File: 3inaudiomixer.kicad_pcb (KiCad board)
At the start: 2 copper layers, 64 x 72 mm, 44 parts, among them J1 AudioJack3, J2 AudioJack3, J3 AudioJack3, J4 AudioJack3, U1 LF353D, U2 LF353D, U3 L78L05_SOT89, U4 L79L05_SOT89

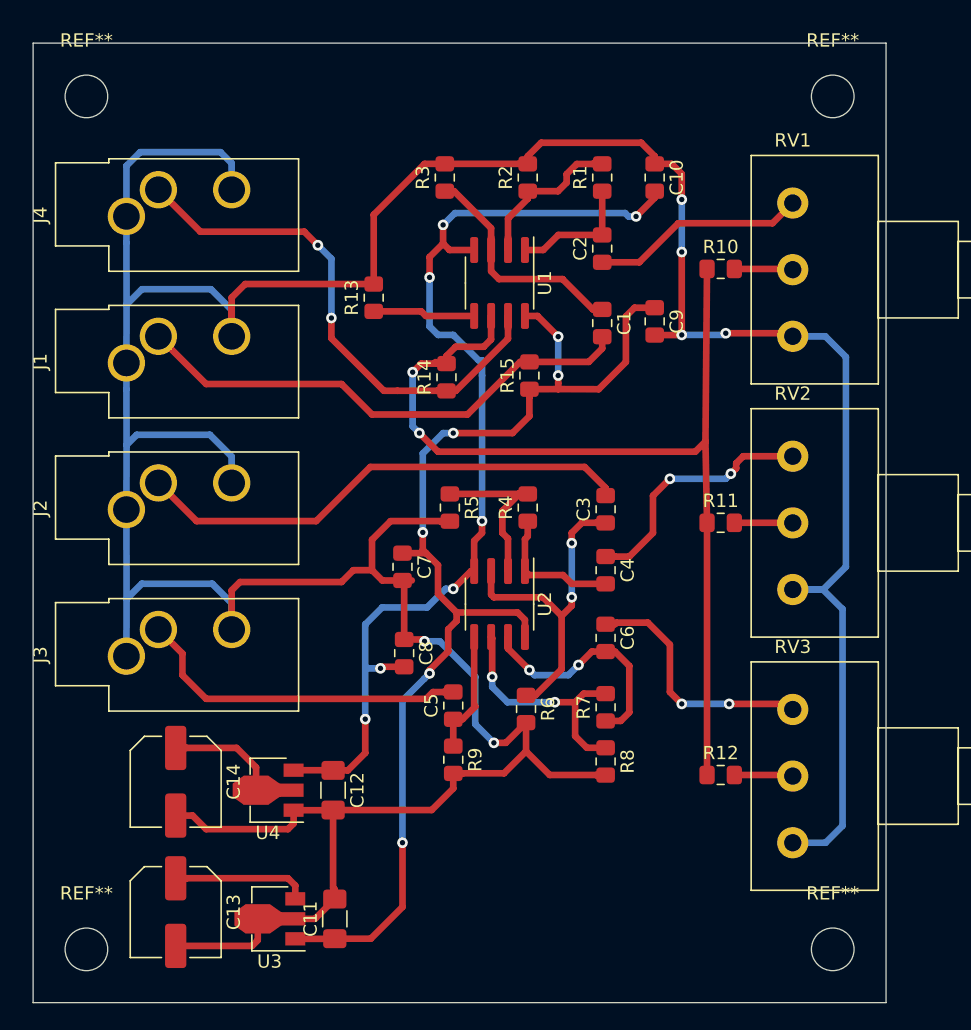
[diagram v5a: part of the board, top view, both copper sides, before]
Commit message: all traces routed & ground planes
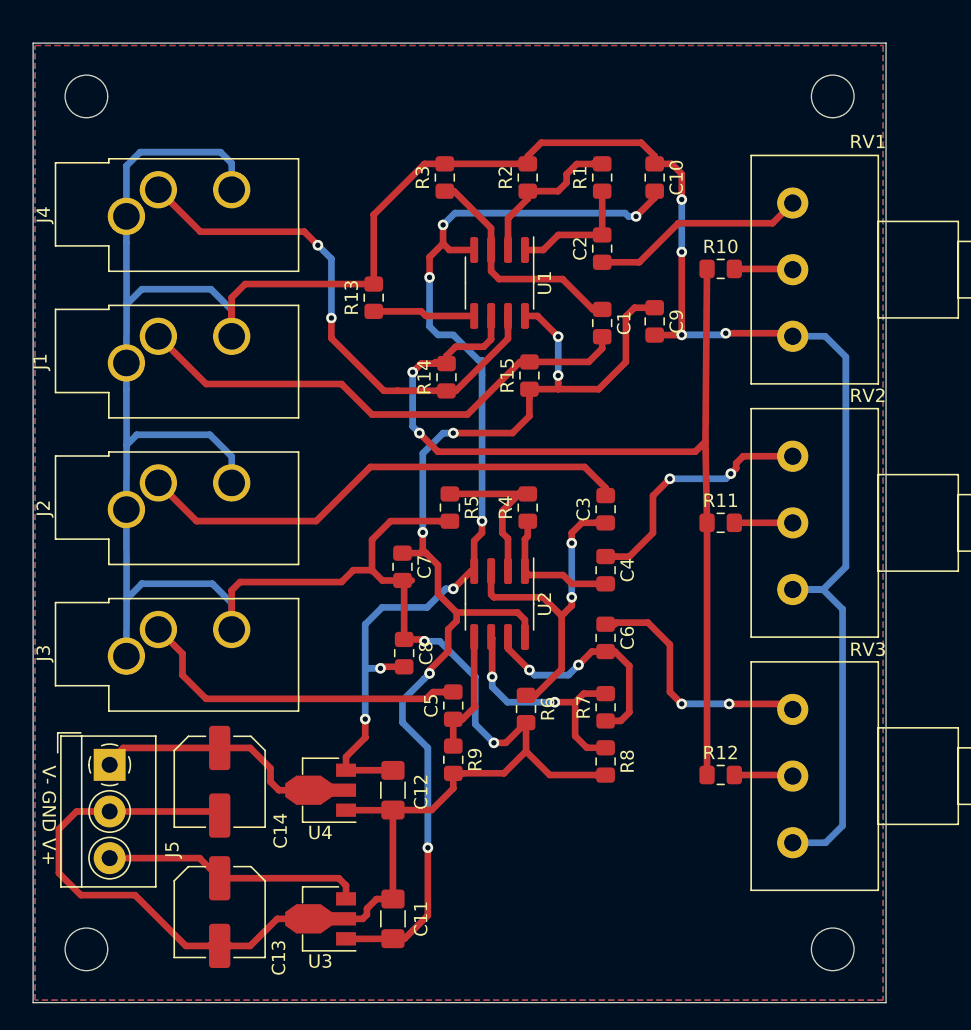
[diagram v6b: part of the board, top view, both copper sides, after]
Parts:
- added J5: Conn_01x03_Female, TerminalBlock_4Ucon:TerminalBlock_4Ucon_1x03_P3.50mm_Horizontal, F.Cu at (118.7, 97.2)
- moved C12 4.49 mm to (140.0, 99.1)
- moved C11 4.36 mm to (140.0, 108.7)
- moved U4 3.94 mm to (135.0, 99.1)
- moved U3 3.81 mm to (135.0, 108.7)
- moved C13 3.30 mm to (127.0, 108.2)
- moved C14 3.30 mm to (127.0, 98.4)
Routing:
- net Net-(C10-Pad1): track 308.7 -> 323.7 mm
- net Net-(C13-Pad1): track 10.2 -> 19.6 mm
- net Net-(C14-Pad1): track 12.4 -> 20.2 mm
- net Net-(C11-Pad1): track 86.4 -> 85.7 mm
- net Net-(C10-Pad2): track 77.5 -> 77.0 mm
- added copper zone on B.Cu, net Net-(C10-Pad1)
- added copper zone on F.Cu, net Net-(C10-Pad1)
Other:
- board text added: "V- GND V+"

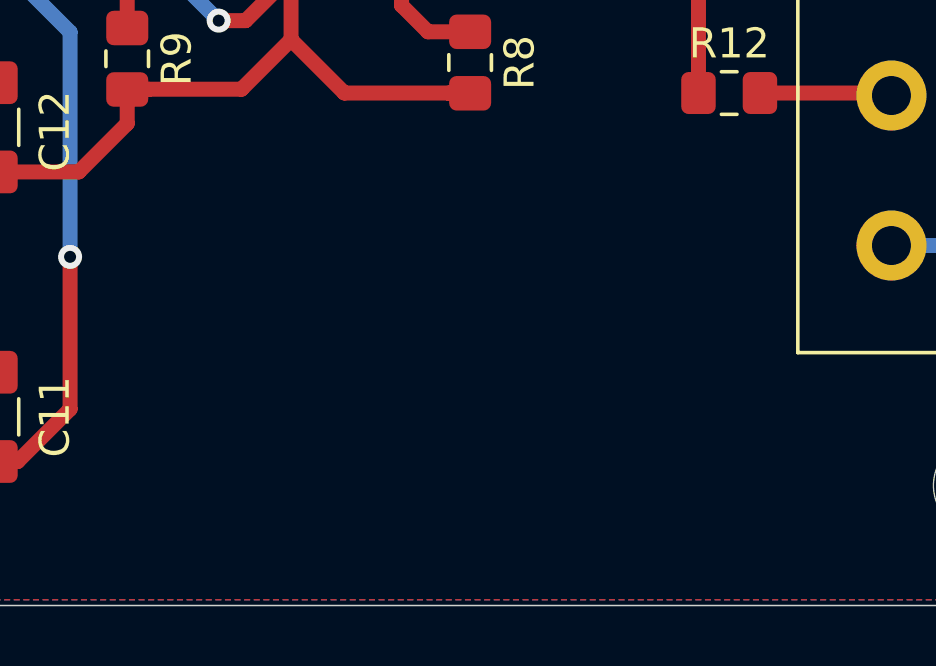
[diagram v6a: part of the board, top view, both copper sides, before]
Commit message: scaled down logo
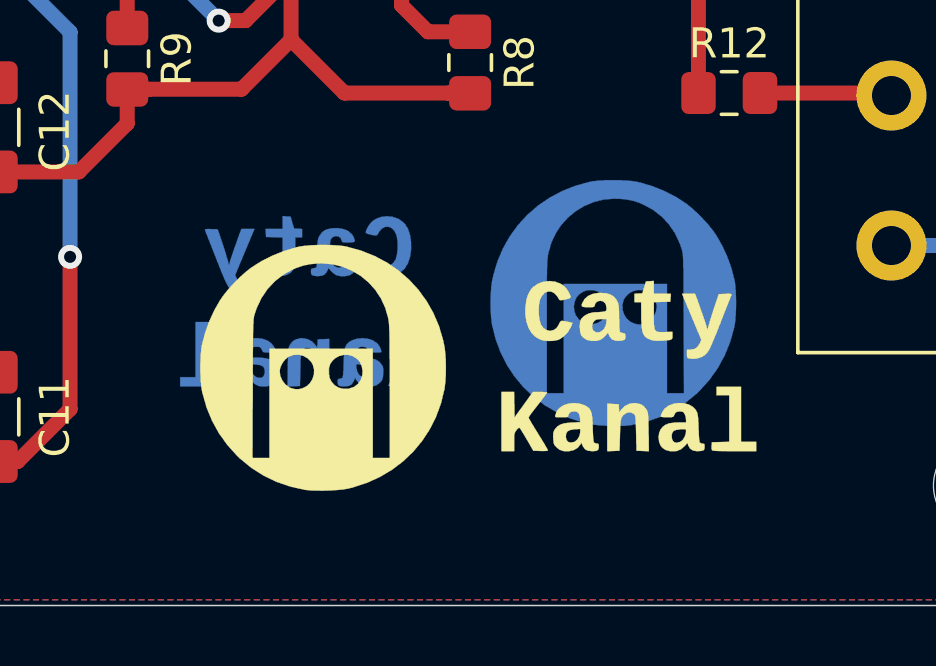
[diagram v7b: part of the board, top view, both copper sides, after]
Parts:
- added G***: LOGO, Logos_Caty_Kanal:CATY-KANAL-Logo_18x8mm_Copper, B.Cu at (155.6, 104.9)
- added G***: LOGO, Logos_Caty_Kanal:CATY-KANAL-Logo_18x8mm_SilkScreen, F.Cu at (156.2, 107.1)

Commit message: pcb finished
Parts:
- added G***: LOGO, Logos_Caty_Kanal:MUSIC-NOTES_9x5mm_SilkScreen, F.Cu at (150.1, 48.1)
- added REF**: SolderWirePad_1x01_Drill0.8mm, Connector_Wire:SolderWirePad_1x01_Drill0.8mm, F.Cu at (166.1, 48.9)
- added REF**: SolderWirePad_1x01_Drill0.8mm, Connector_Wire:SolderWirePad_1x01_Drill0.8mm, F.Cu at (166.1, 108.5)
- moved G*** 2.19 mm to (154.1, 107.4)
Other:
- board text added: "3 INPUT AUDIO MIXER"
- board text added: "IN"
- board text added: "OUT"
